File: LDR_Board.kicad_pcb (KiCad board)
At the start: 2 copper layers, 23 parts, among them J1 Conn_01x07_Pin, J2 Conn_01x02_Pin

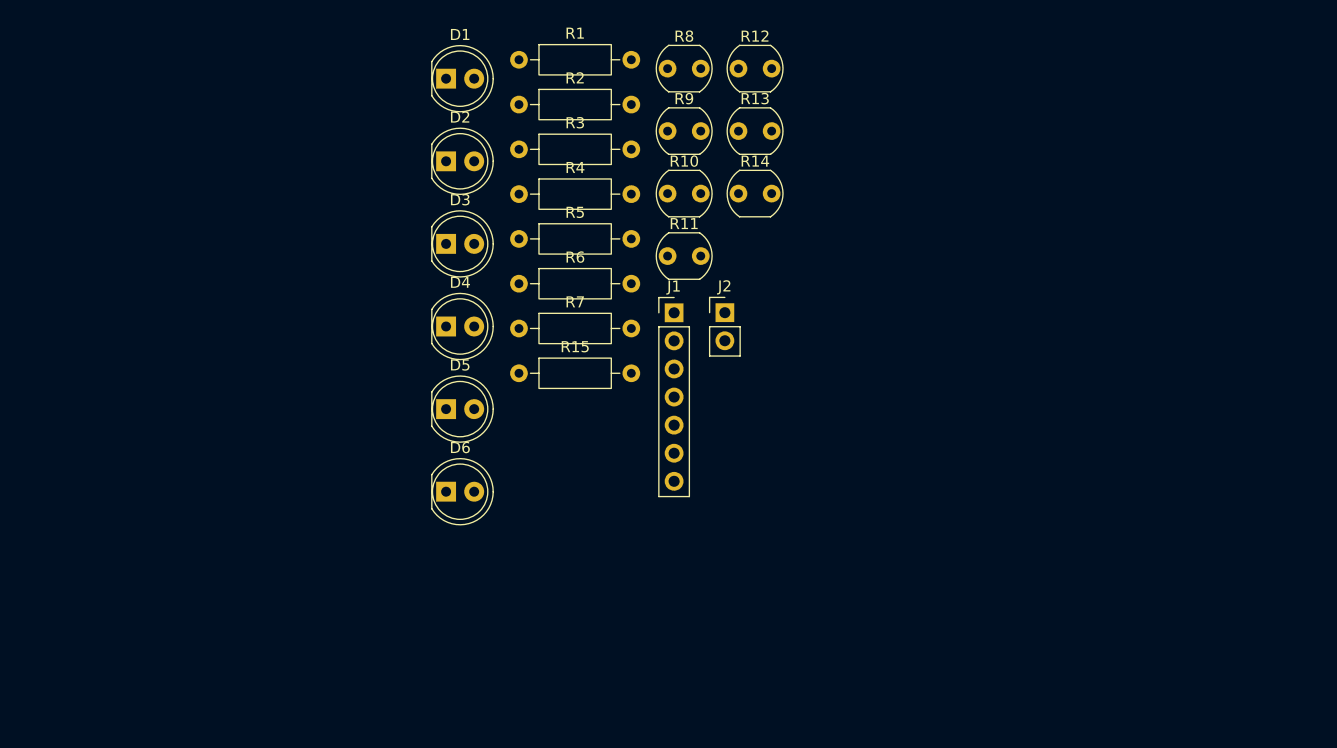
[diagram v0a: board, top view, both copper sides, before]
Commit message: Arranged components
Untangled all the components on the PCB layout and prepared them for running traces. No actual wiring has been done yet.
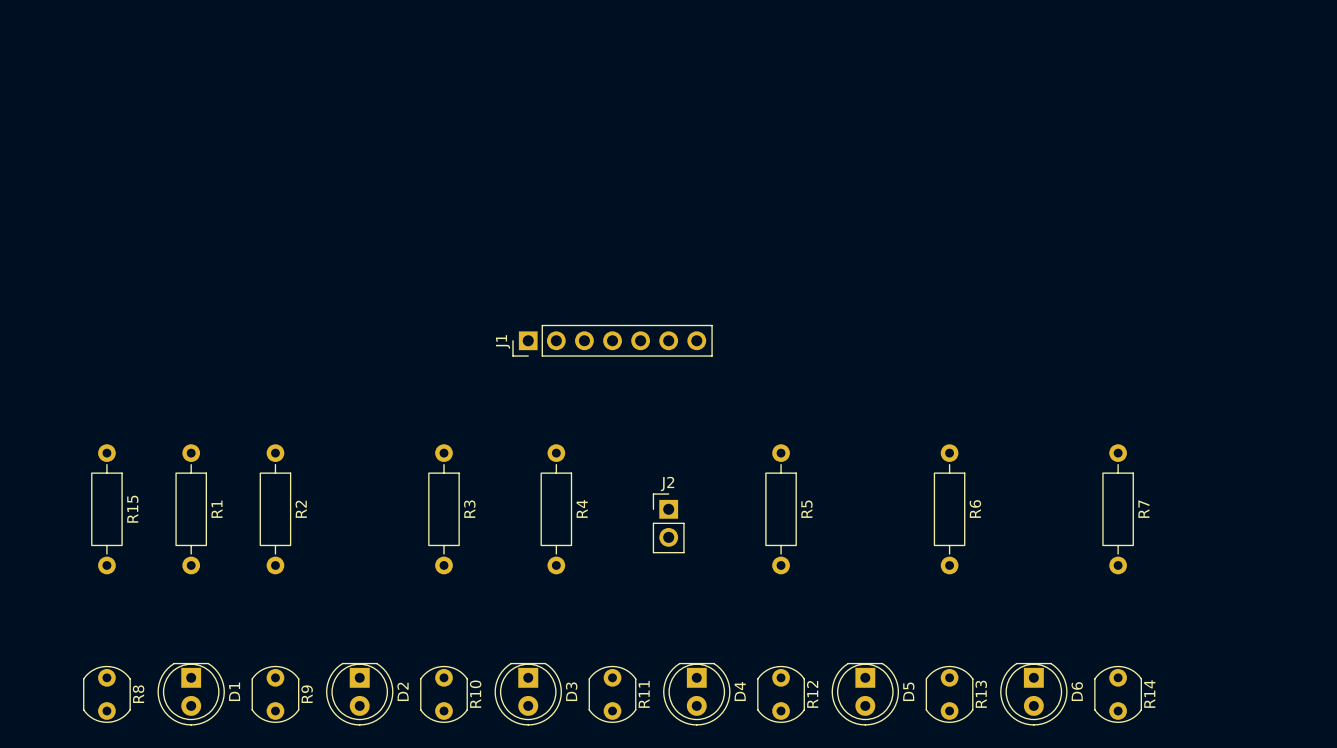
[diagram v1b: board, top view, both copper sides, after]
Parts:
- moved R8 74.9 mm to (104.1, 127.0), turned to -90 degrees
- moved R9 60.8 mm to (119.4, 127.0), turned to -90 degrees
- moved D1 58.9 mm to (111.8, 127.0), turned to -90 degrees
- moved D6 55.8 mm to (188.0, 127.0), turned to -90 degrees
- moved R14 55.6 mm to (195.6, 127.0), turned to -90 degrees
- moved R7 55.3 mm to (195.6, 106.7), turned to -90 degrees
- moved R12 55.2 mm to (165.1, 127.0), turned to -90 degrees
- moved R13 53.0 mm to (180.3, 127.0), turned to -90 degrees
- moved R10 48.2 mm to (134.6, 127.0), turned to -90 degrees
- moved D2 47.4 mm to (127.0, 127.0), turned to -90 degrees
- moved R1 46.3 mm to (111.8, 106.7), turned to -90 degrees
- moved D5 45.0 mm to (172.7, 127.0), turned to -90 degrees
- moved R6 41.8 mm to (180.3, 106.7), turned to -90 degrees
- moved D3 39.9 mm to (142.2, 127.0), turned to -90 degrees
- moved D4 39.0 mm to (157.5, 127.0), turned to -90 degrees
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
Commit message: Routed traces and added silkscreen
Still need to export for manufacturing, but initial design is complete.
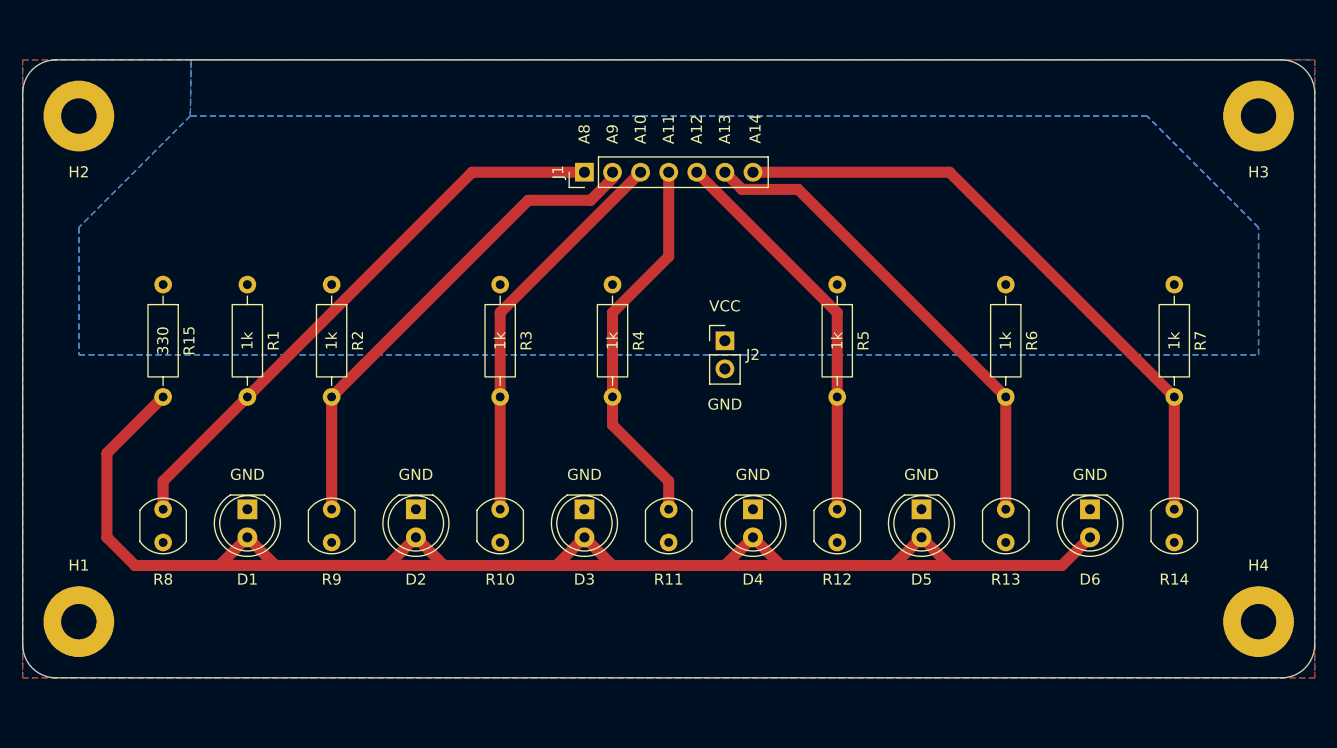
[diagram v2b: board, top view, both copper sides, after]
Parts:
- added G***: LOGO, LOGO, B.Cu at (124.5, 83.8)
- added H1: MountingHole_Pad, MountingHole:MountingHole_3.2mm_M3_Pad, F.Cu at (101.6, 121.9)
- added H2: MountingHole_Pad, MountingHole:MountingHole_3.2mm_M3_Pad, F.Cu at (101.6, 76.2)
- added H3: MountingHole_Pad, MountingHole:MountingHole_3.2mm_M3_Pad, F.Cu at (208.3, 76.2)
- added H4: MountingHole_Pad, MountingHole:MountingHole_3.2mm_M3_Pad, F.Cu at (208.3, 121.9)
- moved J2 16.1 mm to (160.0, 96.5)
- moved R4 16.1 mm to (149.9, 91.4)
- moved R5 16.1 mm to (170.2, 91.4)
- moved R1 16.1 mm to (116.8, 91.4)
- moved R15 16.1 mm to (109.2, 91.4)
- moved R2 16.1 mm to (124.5, 91.4)
- moved R3 16.1 mm to (139.7, 91.4)
- moved R6 16.1 mm to (185.4, 91.4)
- moved R7 16.1 mm to (200.7, 91.4)
- moved D2 16.1 mm to (132.1, 111.8)
- moved D4 16.1 mm to (162.6, 111.8)
- moved D5 16.1 mm to (177.8, 111.8)
- moved R12 16.1 mm to (170.2, 111.8)
- moved D1 16.1 mm to (116.8, 111.8)
- moved R8 16.1 mm to (109.2, 111.8)
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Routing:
- net Net-(D1-A): track 0.00 -> 141.7 mm
- net /A14: track 0.00 -> 56.7 mm
- net /A8: track 0.00 -> 52.2 mm
- net /A9: track 0.00 -> 44.3 mm
- net /A13: track 0.00 -> 44.0 mm
- net /A12: track 0.00 -> 35.7 mm
- net /A10: track 0.00 -> 35.7 mm
- net /A11: track 0.00 -> 34.7 mm
- added copper zone on F.Cu, net (none)
- added copper zone on B.Cu, net GND
- added copper zone on B.Cu, net VCC
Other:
- board outline added: 116.8 x 55.9 mm
- board text added: "1k"
- board text added: "330"
- board text added: "A10"
- board text added: "A11"
- board text added: "A12"
- board text added: "A13"
- board text added: "A14"
- board text added: "A8"
- board text added: "A9"
- board text added: "Connect on this side!"
- board text added: "GND"
- board text added: "University of Washington ECE EE 201 Winter 2026 Section AD Final Project Sensor Array Carefully crafted by: Yung-Ching, Thy, and Yehoshua"
- board text added: "VCC"
